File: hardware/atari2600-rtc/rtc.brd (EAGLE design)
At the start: 15 x 21.2 mm, 4 parts

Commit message: Update RTC design
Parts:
- added G1: CR2032H, battery:CR2032H
- added IC1: DS1307, ic-package:DIL08
- moved R1 33.8 mm to (18.9, 33.0), turned to 270 degrees
- moved R2 25.0 mm to (16.6, 33.0)
- moved X1 22.9 mm to (11.5, 46.9)
- moved C1 18.5 mm to (3.22, 33.1), turned to 270 degrees
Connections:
- new net N$4: G1.+, IC1.3
- net GND: now also G1.-, IC1.4
- net N$1: now also IC1.5
- net N$2: now also IC1.6
- net VCC: now also IC1.8
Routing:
- removed copper zone on layer 1, net GND
- removed copper zone on layer 16, net GND
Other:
- board size 15 x 21.2 mm -> 22.5 x 43.7 mm
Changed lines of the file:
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@@
 <setting verticaltext="up"/>
 </settings>
-<grid distance="0.5" unitdist="mm" unit="mm" style="lines" multiple="1" display="yes" altdistance="5" altunitdist="mil" altunit="mil"/>
+<grid distance="0.1" unitdist="mm" unit="mm" style="lines" multiple="1" display="yes" altdistance="5" altunitdist="mil" altunit="mil"/>
 <layers>
 <layer number="1" name="Top" color="4" fill="1" visible="yes" active="yes"/>
@@
 <board>
 <plain>
-<wire x1="2" y1="0" x2="13" y2="0" width="0" layer="20"/>
-<wire x1="15" y1="2" x2="15" y2="21.2" width="0" layer="20"/>
-<wire x1="15" y1="21.2" x2="0" y2="21.2" width="0" layer="20"/>
-<wire x1="0" y1="21.2" x2="0" y2="2" width="0" layer="20"/>
-<wire x1="2" y1="0" x2="0" y2="2" width="0" layer="20" curve="-90"/>
-<wire x1="15" y1="2" x2="13" y2="0" width="0" layer="20" curve="-90"/>
-<text x="9.5" y="14.5" size="0.3048" layer="25">daltonlabs.pl
-RTC for Atari 2600</text>
-<text x="5.5" y="1" size="0.8128" layer="26" rot="MR90">daltonlabs.pl
+<wire x1="0" y1="0" x2="22.5" y2="0" width="0" layer="20"/>
+<wire x1="22.5" y1="0" x2="22.5" y2="43.7" width="0" layer="20"/>
+<wire x1="22.5" y1="43.7" x2="0" y2="43.7" width="0" layer="20"/>
+<wire x1="0" y1="43.7" x2="0" y2="0" width="0" layer="20"/>
+<text x="9.5" y="23.5" size="0.8128" layer="26" rot="MR90">daltonlabs.pl
 RTC for Atari 2600</text>
 </plain>
@@
 </autorouter>
 <elements>
-<element name="C1" library="rcl" library_urn="urn:adsk.eagle:library:334" package="C025-025X050" package3d_urn="urn:adsk.eagle:package:23629/2" value="100n" x="6.15" y="14.88" smashed="yes" rot="R180">
-<attribute name="POPULARITY" value="65" x="-26.87" y="37.74" size="1.778" layer="27" rot="R180" display="off"/>
-<attribute name="SPICEPREFIX" value="C" x="-26.87" y="37.74" size="1.778" layer="27" rot="R180" display="off"/>
-</element>
-<element name="R1" library="rcl" library_urn="urn:adsk.eagle:library:334" package="0204/7" package3d_urn="urn:adsk.eagle:package:23498/2" value="10k" x="6.07" y="1.7" smashed="yes" rot="R180">
-<attribute name="POPULARITY" value="79" x="-34.57" y="23.29" size="1.778" layer="27" rot="R180" display="off"/>
-<attribute name="SPICEPREFIX" value="R" x="-34.57" y="23.29" size="1.778" layer="27" rot="R180" display="off"/>
-</element>
-<element name="R2" library="rcl" library_urn="urn:adsk.eagle:library:334" package="0204/7" package3d_urn="urn:adsk.eagle:package:23498/2" value="10k" x="12.54" y="8.33" smashed="yes" rot="R90">
-<attribute name="POPULARITY" value="79" x="49.37" y="26.11" size="1.778" layer="27" rot="R90" display="off"/>
-<attribute name="SPICEPREFIX" value="R" x="49.37" y="26.11" size="1.778" layer="27" rot="R90" display="off"/>
-</element>
-<element name="X1" library="con-subd" library_urn="urn:adsk.eagle:library:189" package="F09D" package3d_urn="urn:adsk.eagle:package:10273/1" value="" x="7.52" y="24.44" smashed="yes">
-<attribute name="MF" value="" x="39.27" y="13.01" size="1.778" layer="27" display="off"/>
-<attribute name="MPN" value="" x="39.27" y="13.01" size="1.778" layer="27" display="off"/>
-<attribute name="OC_FARNELL" value="unknown" x="39.27" y="13.01" size="1.778" layer="27" display="off"/>
-<attribute name="OC_NEWARK" value="unknown" x="39.27" y="13.01" size="1.778" layer="27" display="off"/>
-<attribute name="POPULARITY" value="4" x="39.27" y="13.01" size="1.778" layer="27" display="off"/>
-<attribute name="VALUE" x="8.79" y="14.28" size="1.778" layer="27" ratio="10"/>
+<element name="C1" library="rcl" library_urn="urn:adsk.eagle:library:334" package="C025-025X050" package3d_urn="urn:adsk.eagle:package:23629/2" value="100n" x="3.22" y="33.15" smashed="yes" rot="R270">
+<attribute name="POPULARITY" value="65" x="-19.64" y="0.13" size="1.778" layer="27" rot="R270" display="off"/>
+<attribute name="SPICEPREFIX" value="C" x="-19.64" y="0.13" size="1.778" layer="27" rot="R270" display="off"/>
+</element>
+<element name="R1" library="rcl" library_urn="urn:adsk.eagle:library:334" package="0204/7" package3d_urn="urn:adsk.eagle:package:23498/2" value="10k" x="18.9" y="32.97" smashed="yes" rot="R270">
+<attribute name="POPULARITY" value="79" x="-2.69" y="-7.67" size="1.778" layer="27" rot="R270" display="off"/>
+<attribute name="SPICEPREFIX" value="R" x="-2.69" y="-7.67" size="1.778" layer="27" rot="R270" display="off"/>
+</element>
+<element name="R2" library="rcl" library_urn="urn:adsk.eagle:library:334" package="0204/7" package3d_urn="urn:adsk.eagle:package:23498/2" value="10k" x="16.64" y="33.03" smashed="yes" rot="R90">
+<attribute name="POPULARITY" value="79" x="53.47" y="50.81" size="1.778" layer="27" rot="R90" display="off"/>
+<attribute name="SPICEPREFIX" value="R" x="53.47" y="50.81" size="1.778" layer="27" rot="R90" display="off"/>
+</element>
+<element name="X1" library="con-subd" library_urn="urn:adsk.eagle:library:189" package="F09D" package3d_urn="urn:adsk.eagle:package:10273/1" value="" x="11.52" y="46.94" smashed="yes">
+<attribute name="MF" value="" x="43.27" y="35.51" size="1.778" layer="27" display="off"/>
+<attribute name="MPN" value="" x="43.27" y="35.51" size="1.778" layer="27" display="off"/>
+<attribute name="OC_FARNELL" value="unknown" x="43.27" y="35.51" size="1.778" layer="27" display="off"/>
+<attribute name="OC_NEWARK" value="unknown" x="43.27" y="35.51" size="1.778" layer="27" display="off"/>
+<attribute name="POPULARITY" value="4" x="43.27" y="35.51" size="1.778" layer="27" display="off"/>
+<attribute name="VALUE" x="12.79" y="36.78" size="1.778" layer="27" ratio="10"/>
+</element>
+<element name="IC1" library="ic-package" library_urn="urn:adsk.eagle:library:239" package="DIL08" package3d_urn="urn:adsk.eagle:package:29519/2" value="DS1307" x="10" y="33.1" smashed="yes">
+<attribute name="NAME" x="5.166" y="27.179" size="1.27" layer="25" ratio="10" rot="R90"/>
+<attribute name="POPULARITY" value="8" x="10" y="33.1" size="1.778" layer="27" display="off"/>
+<attribute name="VALUE" x="6.444" y="32.465" size="1.27" layer="27" ratio="10"/>
+</element>
+<element name="G1" library="battery" library_urn="urn:adsk.eagle:library:109" package="CR2032H" package3d_urn="urn:adsk.eagle:package:4585/1" value="CR2032H" x="11.2" y="13.6" smashed="yes">
+<attribute name="NAME" x="2.16" y="22.03" size="1.27" layer="25" ratio="10"/>
+<attribute name="POPULARITY" value="0" x="11.2" y="13.6" size="1.778" layer="27" display="off"/>
+<attribute name="VALUE" x="16.28" y="11.695" size="1.27" layer="27" ratio="10" rot="R90"/>
 </element>
 </elements>
@@
 <signal name="VCC">
 <contactref element="X1" pad="7"/>
-<contactref element="R2" pad="2"/>
 <contactref element="R1" pad="2"/>
 <contactref element="C1" pad="1"/>
-<wire x1="7.42" y1="14.88" x2="6.1484" y2="18.3948" width="0" layer="19" extent="16-16"/>
-<wire x1="12.54" y1="12.14" x2="7.42" y2="14.88" width="0" layer="19" extent="1-1"/>
-<wire x1="2.26" y1="1.7" x2="7.42" y2="14.88" width="0" layer="19" extent="1-1"/>
+<contactref element="R2" pad="2"/>
+<contactref element="IC1" pad="8"/>
+<wire x1="3.22" y1="34.42" x2="10.1484" y2="40.8948" width="0" layer="19" extent="16-16"/>
+<wire x1="16.64" y1="36.84" x2="3.22" y2="34.42" width="0" layer="19" extent="1-1"/>
+<wire x1="18.9" y1="29.16" x2="3.22" y2="34.42" width="0" layer="19" extent="1-1"/>
+<wire x1="6.19" y1="36.91" x2="18.9" y2="29.16" width="0" layer="19" extent="1-1"/>
 </signal>
 <signal name="GND">
 <contactref element="X1" pad="8"/>
 <contactref element="C1" pad="2"/>
-<polygon width="0" layer="1">
-<vertex x="-3" y="21.5"/>
-<vertex x="19.5" y="21.5"/>
-<vertex x="20" y="21"/>
-<vertex x="20" y="-1"/>
-<vertex x="-3" y="-1"/>
-</polygon>
-<polygon width="0" layer="16">
-<vertex x="-3.5" y="22"/>
-<vertex x="-3" y="22.5"/>
-<vertex x="25" y="22.5"/>
-<vertex x="25" y="-0.5"/>
-<vertex x="-3.5" y="-0.5"/>
-</polygon>
-<wire x1="4.88" y1="14.88" x2="8.8916" y2="18.3948" width="0" layer="19" extent="16-16"/>
+<contactref element="IC1" pad="4"/>
+<contactref element="G1" pad="-"/>
+<wire x1="3.22" y1="31.88" x2="12.8916" y2="40.8948" width="0" layer="19" extent="16-16"/>
+<wire x1="13.81" y1="29.29" x2="3.22" y2="31.88" width="0" layer="19" extent="1-1"/>
+<wire x1="11.2" y1="6.615" x2="13.81" y2="29.29" width="0" layer="19" extent="1-1"/>
 </signal>
 <signal name="N$1">
 <contactref element="X1" pad="3"/>
 <contactref element="R2" pad="1"/>
-<wire x1="12.54" y1="4.52" x2="7.52" y2="18.395" width="0" layer="19" extent="1-1"/>
+<contactref element="IC1" pad="5"/>
+<wire x1="16.64" y1="29.22" x2="11.52" y2="40.895" width="0" layer="19" extent="1-1"/>
+<wire x1="13.81" y1="36.91" x2="16.64" y2="29.22" width="0" layer="19" extent="1-1"/>
 </signal>
 <signal name="N$2">
 <contactref element="X1" pad="4"/>
 <contactref element="R1" pad="1"/>
-<wire x1="9.88" y1="1.7" x2="10.2634" y2="18.3952" width="0" layer="19" extent="1-1"/>
+<contactref element="IC1" pad="6"/>
+<wire x1="18.9" y1="36.78" x2="14.2634" y2="40.8952" width="0" layer="19" extent="1-1"/>
+<wire x1="11.27" y1="36.91" x2="18.9" y2="36.78" width="0" layer="19" extent="1-1"/>
+</signal>
+<signal name="N$4">
+<contactref element="G1" pad="+"/>
+<contactref element="IC1" pad="3"/>
+<wire x1="16.28" y1="24.395" x2="11.27" y2="29.29" width="0" layer="19" extent="1-1"/>
 </signal>
 </signals>

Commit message: Update RTC design
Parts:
- removed G1: CR2032H, battery:CR2032H
- added Q1: (no value), crystal:TC26V
- added U$1: CR2032, cr2032:CR2032-20MM
- moved C1 0.71 mm to (3.72, 32.6)
- moved IC1 0.71 mm to (10.5, 32.6)
- moved R1 0.71 mm to (19.4, 32.5)
- moved R2 0.71 mm to (17.1, 32.5)
- moved X1 0.71 mm to (12.0, 46.4)
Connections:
- new net N$3: IC1.3, U$1.VCC
- new net N$5: IC1.1, Q1.2
- net GND: now also U$1.GND; no longer G1.-
- net N$4: now also IC1.2, Q1.1; no longer G1.+, IC1.3
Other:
- board size 22.5 x 43.7 mm -> 23.5 x 42.7 mm

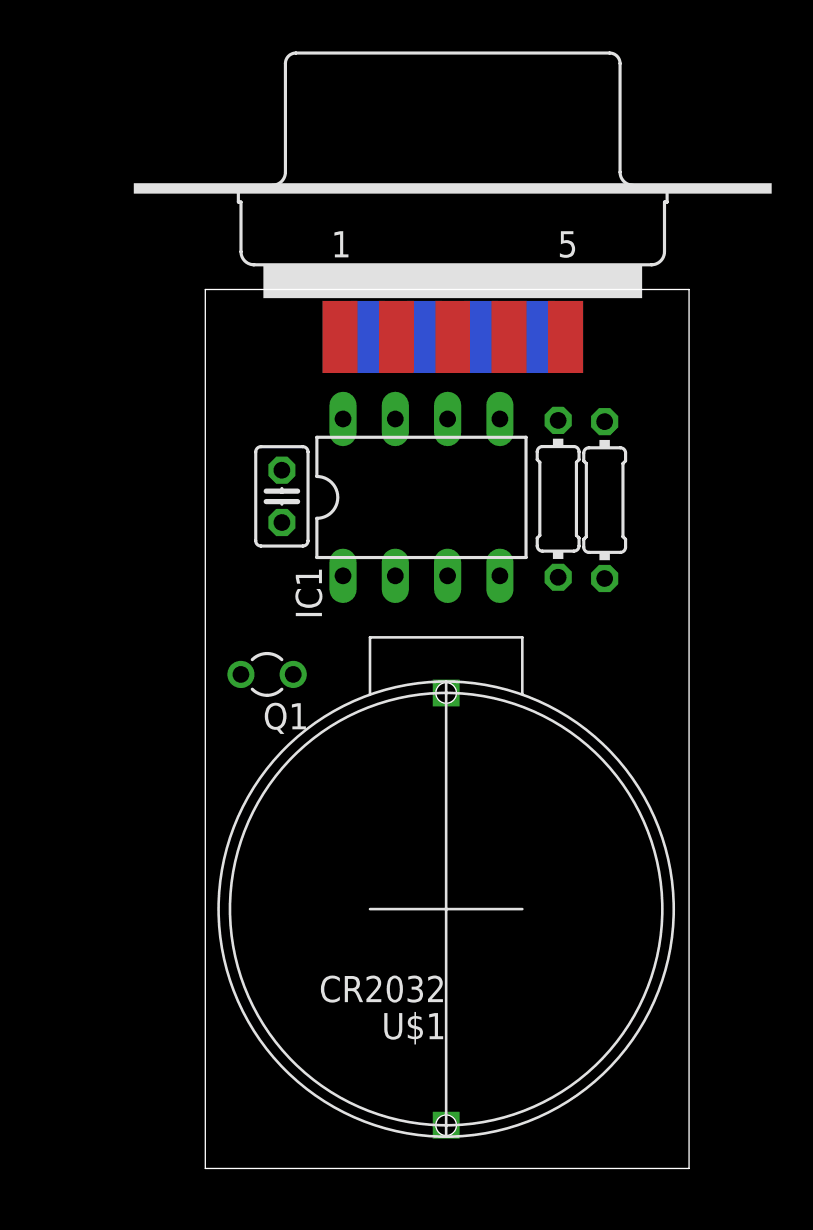
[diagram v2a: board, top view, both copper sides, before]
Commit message: Change battery socket in RTC design
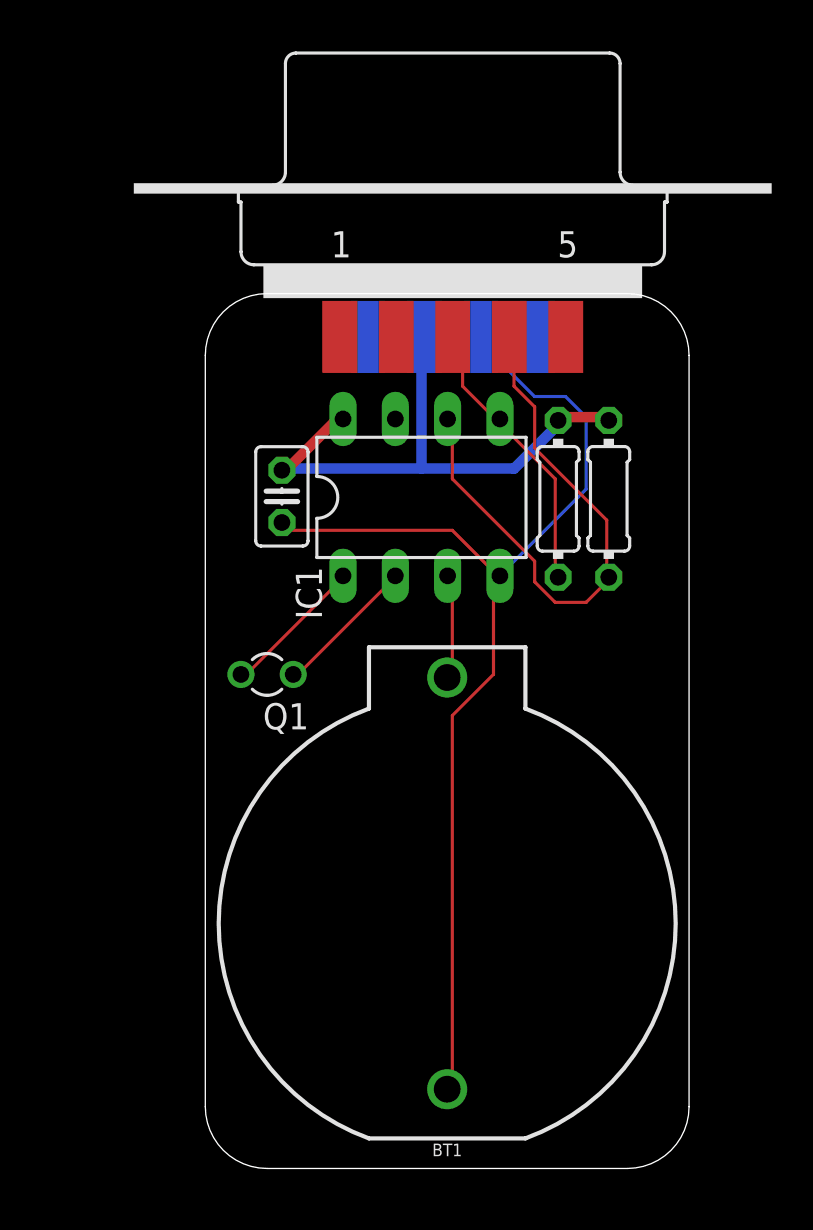
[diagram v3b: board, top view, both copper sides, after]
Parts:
- removed U$1: CR2032, cr2032:CR2032-20MM
- added BT1: (no value), SparkFun-Batteries:BATTCOM_20MM_PTH
- moved R1 0.21 mm to (19.6, 32.5), turned to 90 degrees
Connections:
- net GND: now also BT1.2; no longer U$1.GND
- net N$3: now also BT1.1; no longer U$1.VCC
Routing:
- net GND: track 0.00 -> 54.0 mm
- net N$2: track 0.00 -> 27.8 mm
- net VCC: track 0.00 -> 27.5 mm
- net N$1: track 0.00 -> 13.9 mm
- net N$5: track 0.00 -> 6.98 mm
- net N$4: track 0.00 -> 6.96 mm
- net N$3: track 0.00 -> 5.16 mm
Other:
- board size 23.5 x 42.7 mm -> 23.5 x 42.5 mm
